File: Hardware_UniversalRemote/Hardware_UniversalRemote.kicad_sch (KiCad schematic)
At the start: 6 parts, among them J1 USB_B_Micro, U1 LM1117T-3.3

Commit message: add power block
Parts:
- added D2: LED, symbol Device:LED
- added Q1: S8050, Package_TO_SOT_THT:TO-92_Inline, symbol Transistor_BJT:S8050
- added R1: 22R, symbol Device:R
- C1: footprint (none) -> Capacitor_THT:CP_Radial_D5.0mm_P2.00mm
- C2: footprint (none) -> Capacitor_THT:CP_Radial_D8.0mm_P3.50mm
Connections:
- net +5V: now also R1.1
- net GND: now also Q1.1 (E)
- new net: D2.1 (K), Q1.3 (C)
- new net: D2.2 (A), R1.2

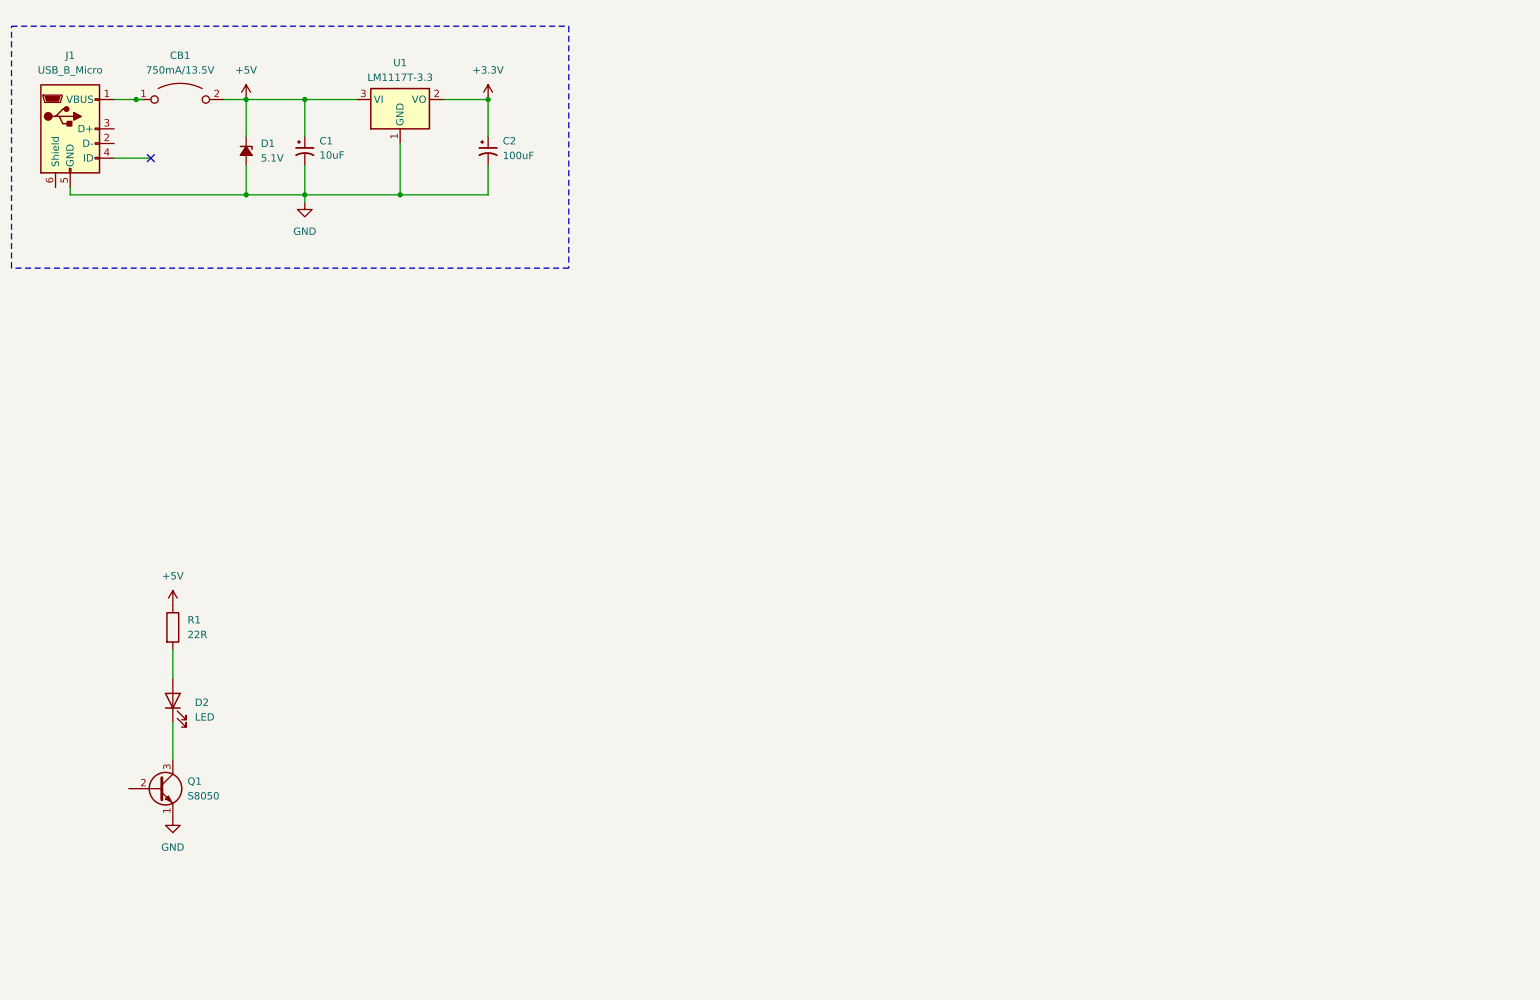
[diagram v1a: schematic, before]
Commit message: add IR emitter block
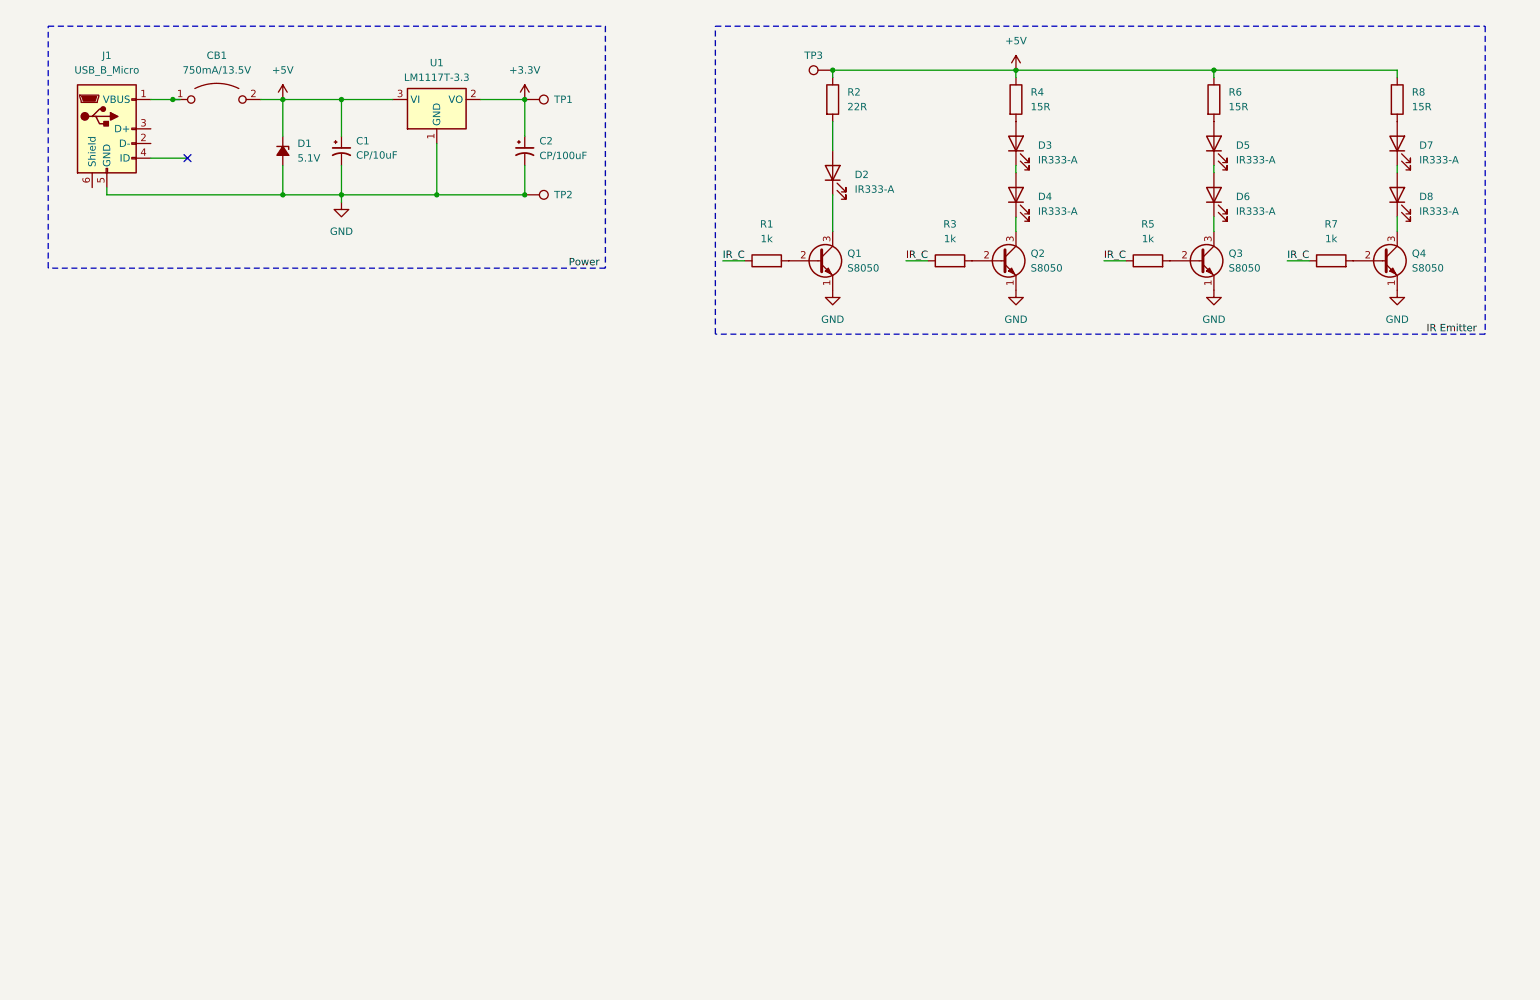
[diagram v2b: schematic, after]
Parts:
- added D3, D4, D5, D6, D7, D8: IR333-A, symbol Device:LED
- added Q2, Q3, Q4: S8050, Package_TO_SOT_THT:TO-92_Inline, symbol Transistor_BJT:S8050
- added R1, R3, R5, R7: 1k, symbol Device:R
- added R4, R6, R8: 15R, symbol Device:R
- added TP1, TP2, TP3: TestPoint, symbol Connector:TestPoint
- C1: value 10uF -> CP/10uF
- C2: value 100uF -> CP/100uF
- D2: value LED -> IR333-A
- renumbered R1 to R2
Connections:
- net +3.3V: now also TP1.1
- net +5V: now also R4.1, R6.1, R8.1, TP3.1
- net GND: now also Q2.1 (E), Q3.1 (E), Q4.1 (E), TP2.1
- net at Q1.2 (B): now also R1.2
- new net: Q2.2 (B), R3.2
- new net: D4.1 (K), Q2.3 (C)
- new net: D3.1 (K), D4.2 (A)
- new net: D3.2 (A), R4.2
- new net: D7.1 (K), D8.2 (A)
- new net: D7.2 (A), R8.2
- new net: Q3.2 (B), R5.2
- new net: Q4.2 (B), R7.2
- new net: D5.1 (K), D6.2 (A)
- new net: D5.2 (A), R6.2
- new net: D8.1 (K), Q4.3 (C)
- new net: D6.1 (K), Q3.3 (C)
- new net IR_C: R1.1, R3.1, R5.1, R7.1
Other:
- moved on the sheet: C1, C2, CB1, D1, D2, J1, Q1, R2, U1

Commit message: add mcu
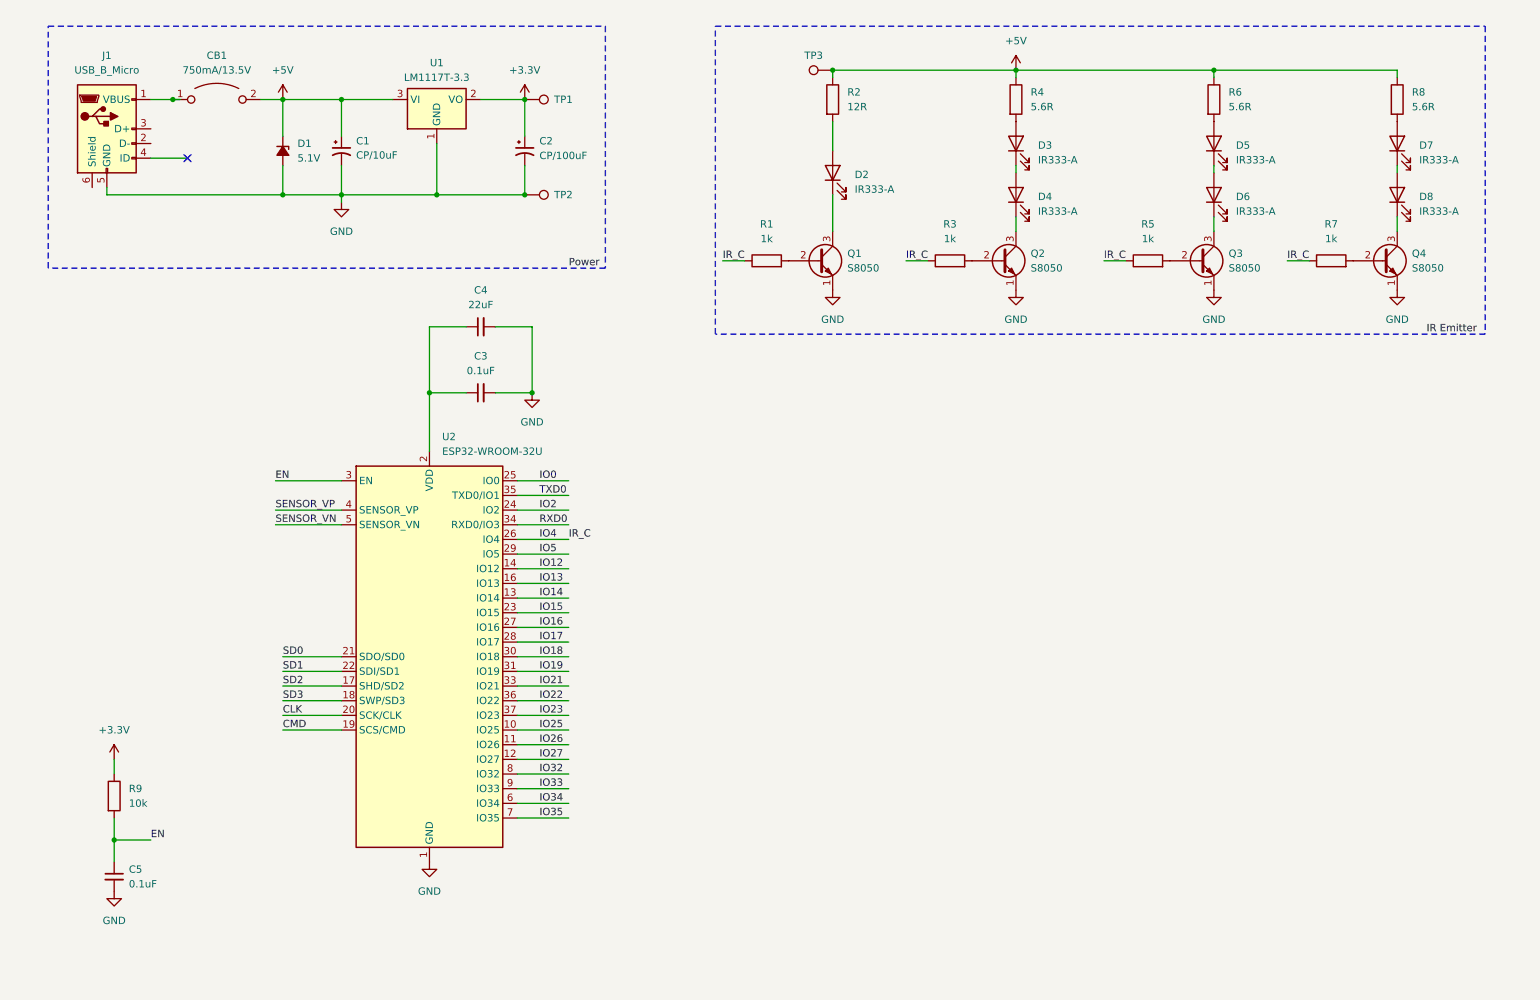
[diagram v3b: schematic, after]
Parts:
- added C3, C5: 0.1uF, symbol Device:C_Small
- added C4: 22uF, symbol Device:C_Small
- added R9: 10k, symbol Device:R
- added U2: ESP32-WROOM-32U, RF_Module:ESP32-WROOM-32U, symbol RF_Module:ESP32-WROOM-32U
- R2: value 22R -> 12R
- R4, R6, R8: value 15R -> 5.6R
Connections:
- net +3.3V: now also R9.1
- net GND: now also C3.2, C4.2, C5.2, U2.1 (GND), U2.15 (GND), U2.38 (GND), U2.39 (GND)
- net IR_C renamed IO4
- net IO4: now also U2.26 (IO4)
- new net: C3.1, C4.1, U2.2 (VDD)
- new net CLK: U2.20 (SCK/CLK)
- new net CMD: U2.19 (SCS/CMD)
- new net EN: C5.1, R9.2, U2.3 (EN)
- new net IO0: U2.25 (IO0)
- new net IO12: U2.14 (IO12)
- new net IO13: U2.16 (IO13)
- new net IO14: U2.13 (IO14)
- new net IO15: U2.23 (IO15)
- new net IO16: U2.27 (IO16)
- new net IO17: U2.28 (IO17)
- new net IO18: U2.30 (IO18)
- new net IO19: U2.31 (IO19)
- new net IO2: U2.24 (IO2)
- new net IO21: U2.33 (IO21)
- new net IO22: U2.36 (IO22)
- new net IO23: U2.37 (IO23)
- new net IO25: U2.10 (IO25)
- new net IO26: U2.11 (IO26)
- new net IO27: U2.12 (IO27)
- new net IO32: U2.8 (IO32)
- new net IO33: U2.9 (IO33)
- new net IO34: U2.6 (IO34)
- new net IO35: U2.7 (IO35)
- new net IO5: U2.29 (IO5)
- new net RXD0: U2.34 (RXD0/IO3)
- new net SD0: U2.21 (SDO/SD0)
- new net SD1: U2.22 (SDI/SD1)
- new net SD2: U2.17 (SHD/SD2)
- new net SD3: U2.18 (SWP/SD3)
- new net SENSOR_VN: U2.5 (SENSOR_VN)
- new net SENSOR_VP: U2.4 (SENSOR_VP)
- new net TXD0: U2.35 (TXD0/IO1)

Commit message: add buttons and usb-uart block
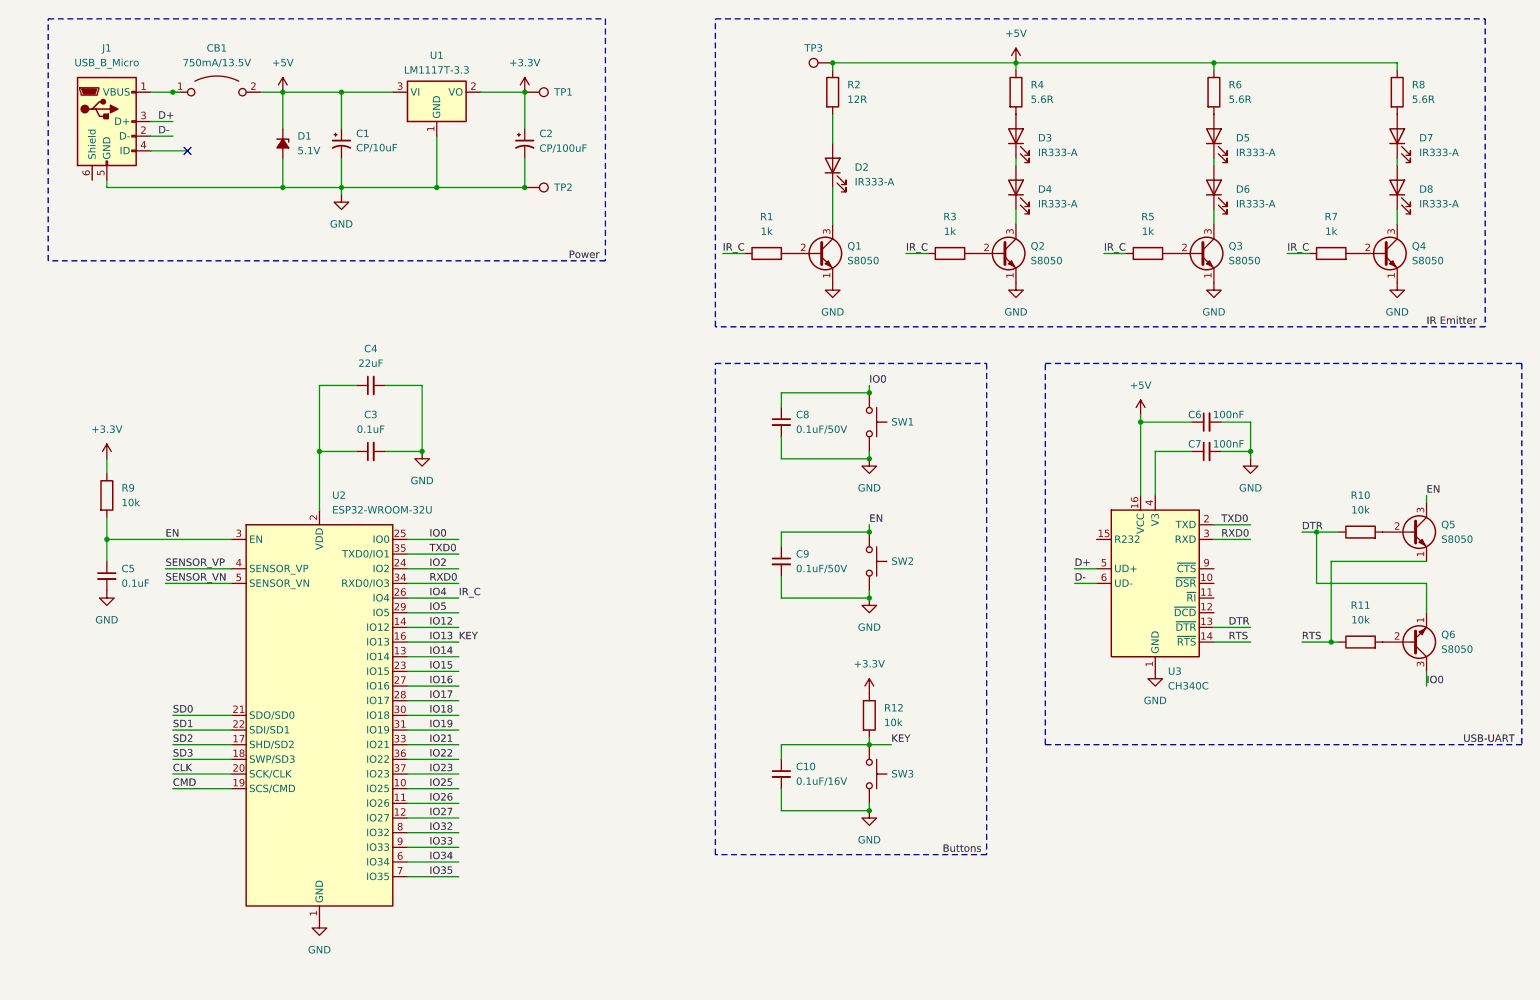
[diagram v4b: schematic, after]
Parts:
- added C10: 0.1uF/16V, symbol Device:C_Small
- added C6, C7: 100nF, symbol Device:C_Small
- added C8, C9: 0.1uF/50V, symbol Device:C_Small
- added Q5, Q6: S8050, Package_TO_SOT_THT:TO-92_Inline, symbol Transistor_BJT:S8050
- added R10, R11, R12: 10k, symbol Device:R
- added SW1, SW2, SW3: SW_Push, symbol Switch:SW_Push
- added U3: CH340C, Package_SO:SOIC-16_3.9x9.9mm_P1.27mm, symbol Interface_USB:CH340C
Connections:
- net +3.3V: now also R12.1
- net +5V: now also C6.1, U3.16 (VCC)
- net EN: now also C9.1, Q5.3 (C), SW2.1
- net GND: now also C10.2, C6.2, C7.2, C8.2, C9.2, SW1.2, SW2.2, SW3.2, U3.1 (GND)
- net IO0: now also C8.1, Q6.3 (C), SW1.1
- net IO13: now also C10.1, R12.2, SW3.1
- net RXD0: now also U3.3 (RXD)
- net TXD0: now also U3.2 (TXD)
- net D-: now reaches J1.2 (D-)
- net D-: now also U3.6 (UD-)
- net D+: now reaches J1.3 (D+)
- net D+: now also U3.5 (UD+)
- new net: C7.1, U3.4 (V3)
- new net: Q5.2 (B), R10.2
- new net: Q6.2 (B), R11.2
- new net DTR: Q6.1 (E), R10.1, U3.13 (~{DTR})
- new net RTS: Q5.1 (E), R11.1, U3.14 (~{RTS})
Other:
- moved on the sheet: C1, C2, C3, C4, C5, CB1, D1, D2, D3, D4, D5, D6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

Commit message: add mcu and ir receiver block
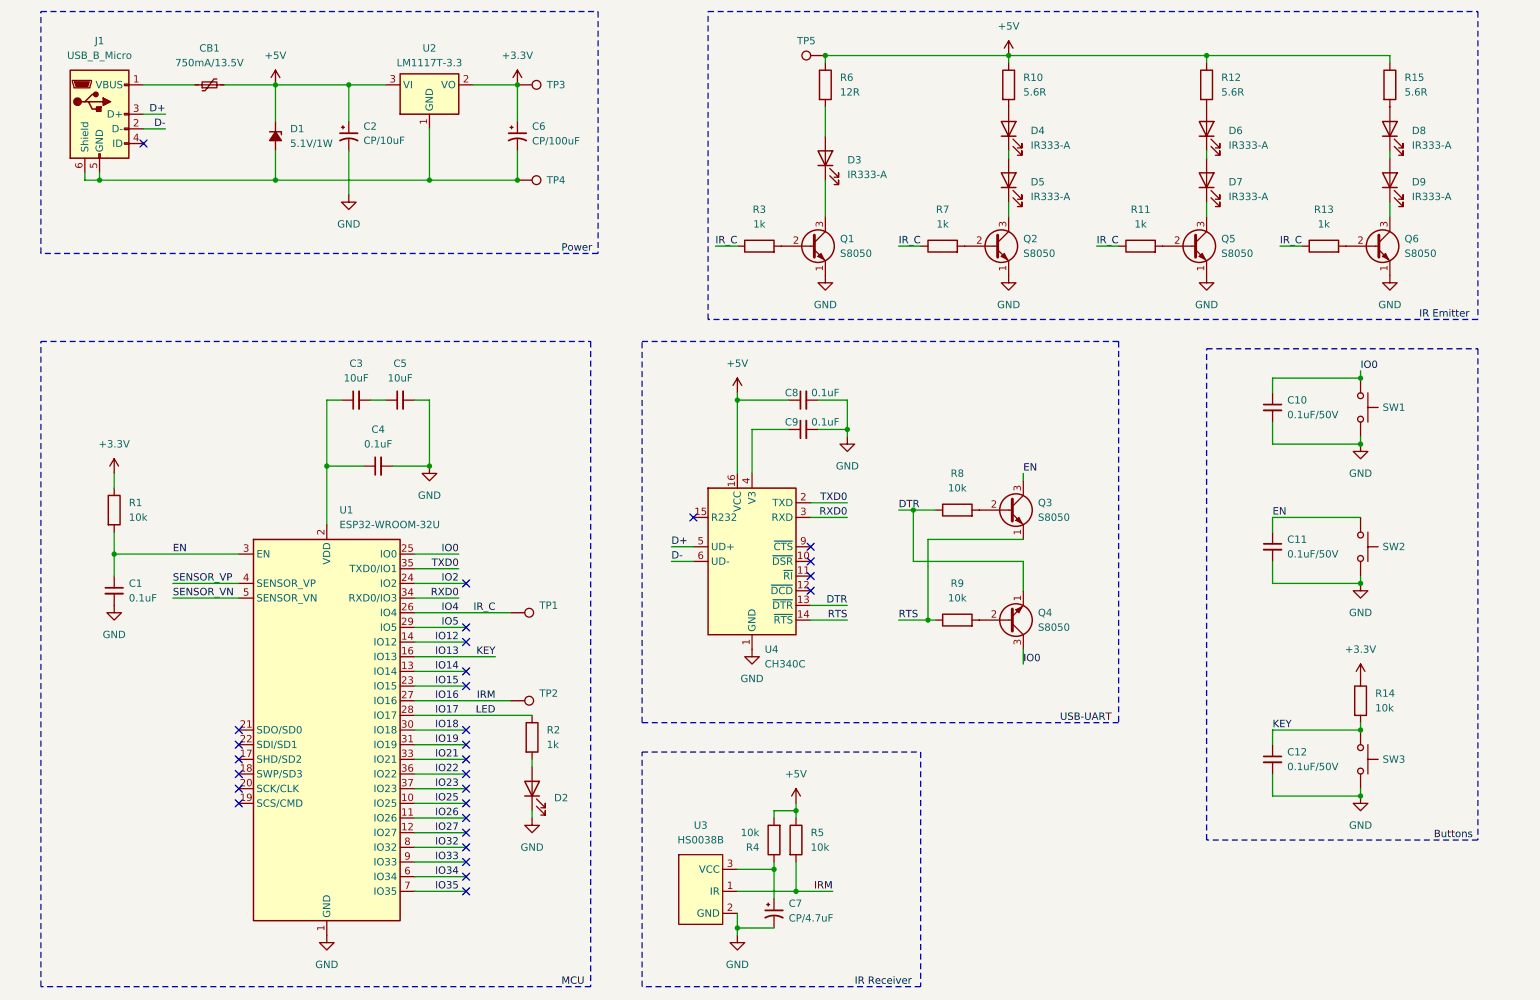
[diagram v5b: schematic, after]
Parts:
- added C5: 10uF, symbol Device:C_Small
- added C7: CP/4.7uF, symbol Device:C_Polarized_Small_US
- added D2: LED, symbol Device:LED
- added R2: 1k, symbol Device:R
- added R4, R5: 10k, symbol Device:R
- added TP1, TP2: TestPoint, symbol Connector:TestPoint
- added U3: HS0038B, symbol HS0038B:HS0038B
- C12: renamed from C10; value 0.1uF/16V -> 0.1uF/50V
- C3: renamed from C4; value 22uF -> 10uF
- C8: renamed from C6; value 100nF -> 0.1uF
- C9: renamed from C7; value 100nF -> 0.1uF
- CB1: symbol Device:CircuitBreaker_1P_US -> Device:Polyfuse_Small
- D1: value 5.1V -> 5.1V/1W
- renumbered C5 to C1, C8 to C10, C9 to C11, C1 to C2, C3 to C4, C2 to C6, D2 to D3, D3 to D4, D4 to D5, D5 to D6, D6 to D7, D7 to D8, D8 to D9, Q5 to Q3, Q6 to Q4, Q3 to Q5, Q4 to Q6, R9 to R1, R4 to R10, R5 to R11, R6 to R12, R7 to R13, R12 to R14, R8 to R15, R1 to R3, R2 to R6, R3 to R7, R10 to R8, R11 to R9, TP1 to TP3, TP2 to TP4, TP3 to TP5, U2 to U1, U1 to U2, U3 to U4
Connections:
- net +5V: now also R4.2, R5.1
- net GND: now also C5.2, C7.2, D2.1 (K), U3.2 (GND); no longer C3.2, C6.2, D1.2 (A), J1.5 (GND), TP4.1, U2.1 (GND)
- net IO16: now also R5.2, TP2.1, U3.1 (IR)
- net IO17: now also R2.1
- net IO4: now also TP1.1
- net at J1.6 (Shield): now also C6.2, D1.2 (A), J1.5 (GND), TP4.1, U2.1 (GND)
- net CLK: no longer names the net of U1.20 (SCK/CLK)
- net CMD: no longer names the net of U1.19 (SCS/CMD)
- net SD0: no longer names the net of U1.21 (SDO/SD0)
- net SD1: no longer names the net of U1.22 (SDI/SD1)
- net SD2: no longer names the net of U1.17 (SHD/SD2)
- net SD3: no longer names the net of U1.18 (SWP/SD3)
- new net: D2.2 (A), R2.2
- new net: C7.1, R4.1, U3.3 (VCC)
- new net: C3.2, C5.1
- no-connect marks 1 -> 29
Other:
- moved on the sheet: C1, C10, C11, C12, C2, C3, C4, C6, C8, C9, D1, D3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
